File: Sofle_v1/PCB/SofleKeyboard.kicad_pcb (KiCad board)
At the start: 2 copper layers, 137.2 x 109.2 mm, 87 parts, among them J1 LED, J2 4PIN, J3 OLED, P1 i2c_pin, P2 i2c_pin, SW1 SW_PUSH, SW10 SW_PUSH, SW11 SW_PUSH, SW12 SW_PUSH, SW13 SW_PUSH, SW14 SW_PUSH, SW15 SW_PUSH, SW16 SW_PUSH, SW17 SW_PUSH, SW18 SW_PUSH, SW19 SW_PUSH, SW2 SW_PUSH, SW20 SW_PUSH, SW21 SW_PUSH, SW22 SW_PUSH, SW23 SW_PUSH, SW24 SW_PUSH, SW25 Rotary_Encoder_Switch, SW26 SW_PUSH, SW27 SW_PUSH, SW28 SW_PUSH, SW29 SW_PUSH, SW3 SW_PUSH, SW30 SW_PUSH, SW4 SW_PUSH, SW5 SW_PUSH, SW6 SW_PUSH, SW7 SW_PUSH, SW8 SW_PUSH, SW9 SW_PUSH, U1 ProMicro

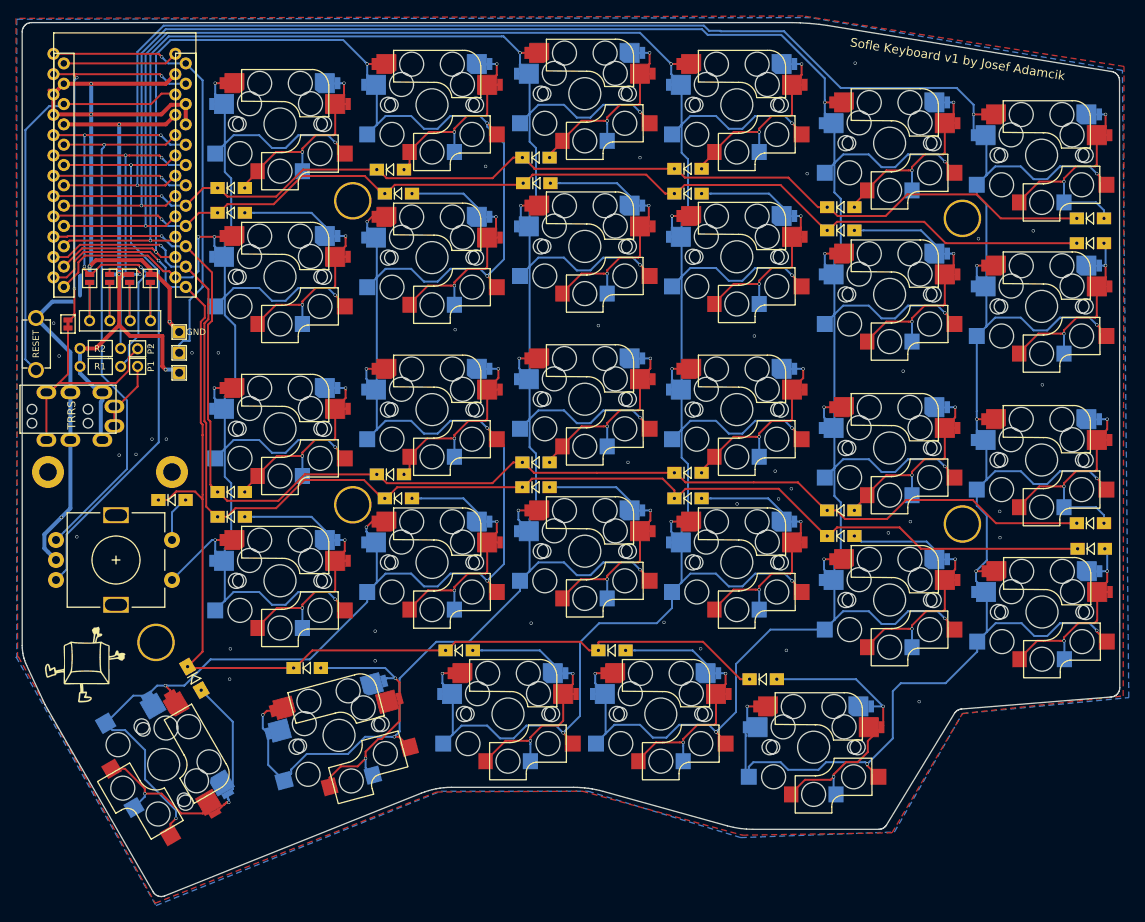
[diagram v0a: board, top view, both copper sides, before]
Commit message: Removed kailh support from the switch footprint
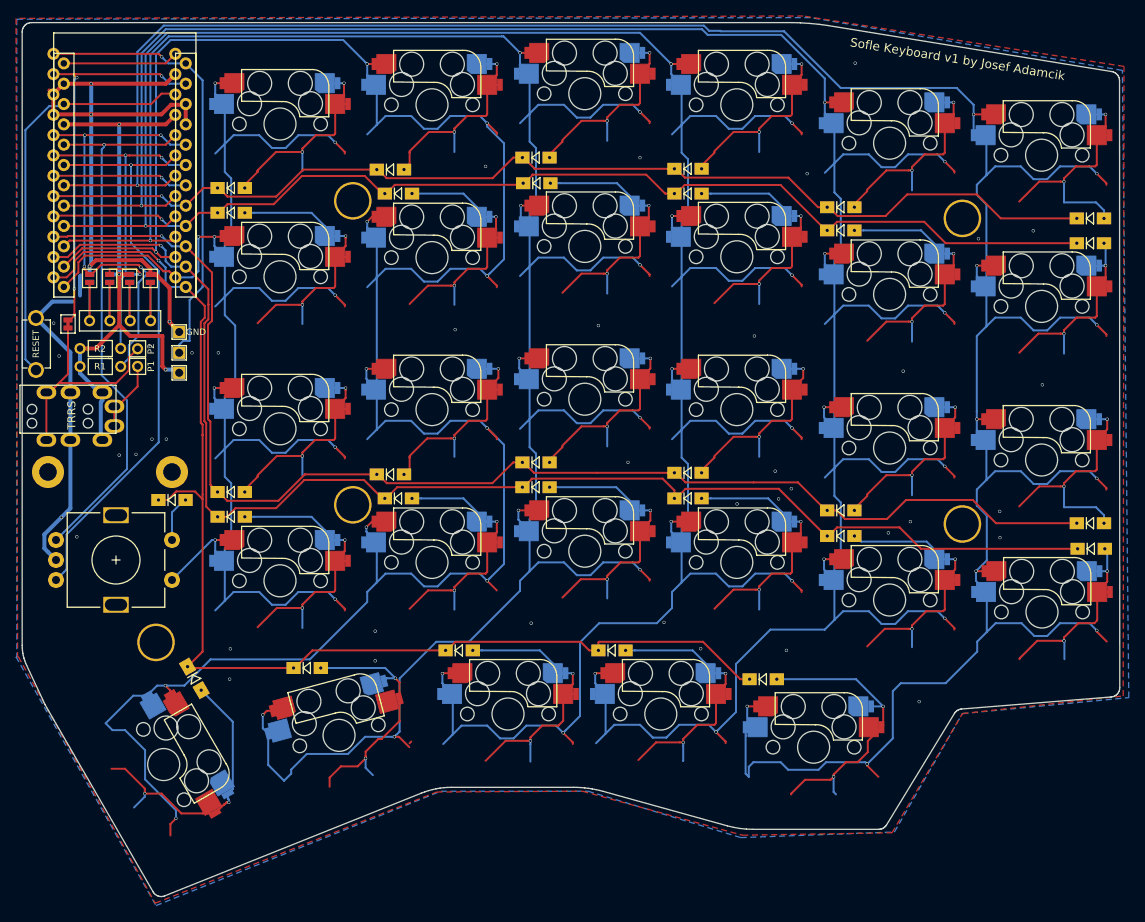
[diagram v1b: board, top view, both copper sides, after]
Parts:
- removed Ref** (x2): Val**, SofleKeyboard-footprint:SofleLogoSmall
- SW1, SW10, SW11, SW12, SW13, SW14, SW15, SW16, SW17, SW18, SW19, SW2, SW20, SW21, SW22, SW23, SW24, SW27, SW28, SW29, SW3, SW30, SW4, SW5, SW6, SW7, SW8, SW9: footprint SofleKeyboard-footprint:CherryMX_KailhLowProfile_Hotswap -> SofleKeyboard-footprint:CherryMX_Hotswap
- SW26: footprint SofleKeyboard-footprint:CherryMX_KailhLowProfile_Hotswap_1.5 -> SofleKeyboard-footprint:CherryMX_Hotswap

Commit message: Fixed routing after footprint change
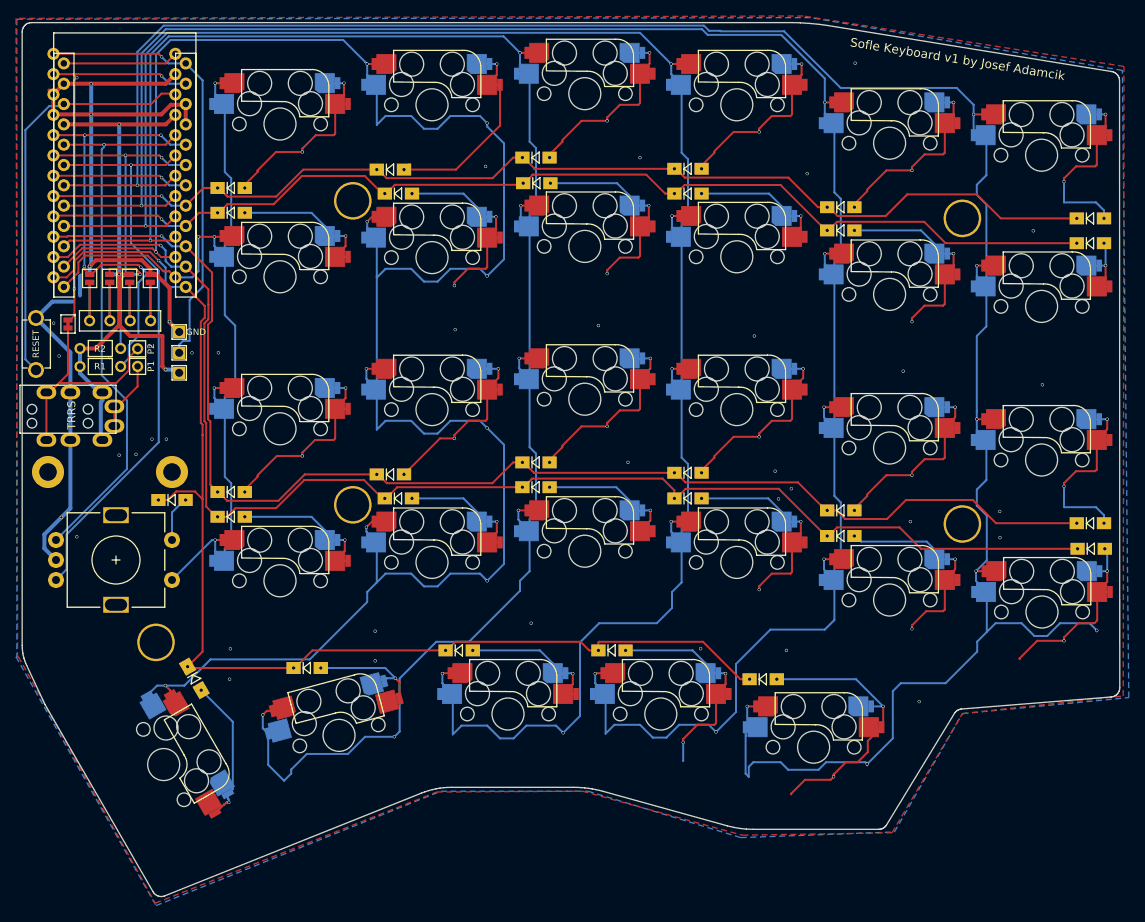
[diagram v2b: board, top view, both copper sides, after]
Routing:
- net SW25A: track 206.1 -> 122.8 mm, vias 9 -> 5
- net col1: track 350.6 -> 270.6 mm, vias 11 -> 7
- net col2: track 334.4 -> 254.3 mm, vias 11 -> 7
- net col3: track 314.7 -> 235.5 mm, vias 11 -> 7
- net col0: track 358.0 -> 300.7 mm, vias 11 -> 8
- net col4: track 311.0 -> 273.0 mm, vias 11 -> 10
- net Net-(D27-Pad2): track 32.8 -> 14.2 mm, vias 2 -> 1
- net Net-(D19-Pad2): track 37.2 -> 19.1 mm, vias 2 -> 1
- net Net-(D12-Pad2): track 28.0 -> 9.92 mm, vias 2 -> 1
- net Net-(D10-Pad2): track 37.0 -> 18.9 mm, vias 2 -> 1
- net Net-(D28-Pad2): track 37.1 -> 19.1 mm, vias 2 -> 1
- net Net-(D21-Pad2): track 37.2 -> 19.2 mm, vias 2 -> 1
- net Net-(D20-Pad2): track 35.2 -> 17.2 mm, vias 2 -> 1
- net Net-(D7-Pad2): track 37.3 -> 19.3 mm, vias 2 -> 1
- net Net-(D26-Pad2): track 36.4 -> 18.5 mm, vias 2 -> 1
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
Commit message: Done with the scheme and positioning of the footprints. Started drawing the tracks
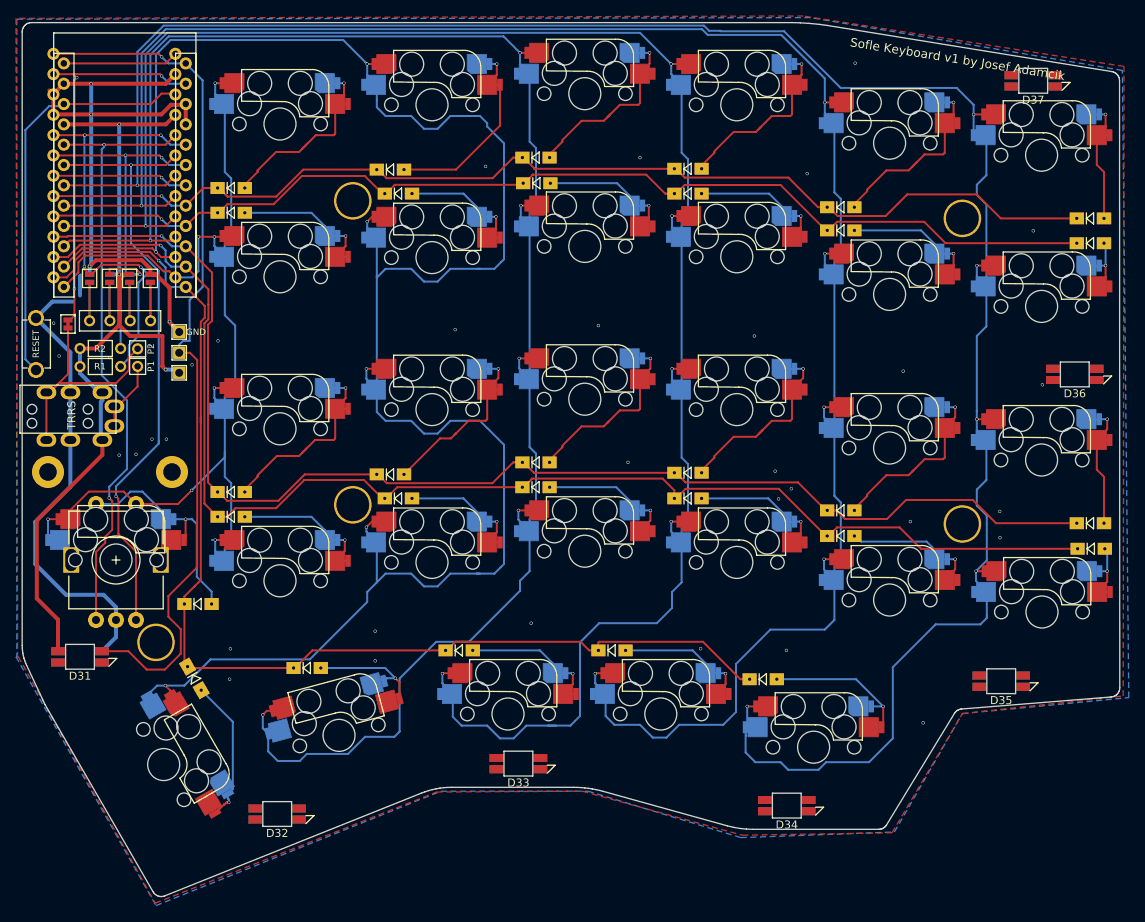
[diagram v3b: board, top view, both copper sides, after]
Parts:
- added D31: SK6812MINI, footprints:YS-SK6812MINI-E_backlight, F.Cu at (95.5, 116.6)
- added D32: SK6812MINI, footprints:YS-SK6812MINI-E_backlight, F.Cu at (120.2, 136.2)
- added D33: SK6812MINI, footprints:YS-SK6812MINI-E_backlight, F.Cu at (150.3, 129.9)
- added D34: SK6812MINI, footprints:YS-SK6812MINI-E_backlight, F.Cu at (183.8, 135.2)
- added D35: SK6812MINI, footprints:YS-SK6812MINI-E_backlight, F.Cu at (210.7, 119.7)
- added D36: SK6812MINI, footprints:YS-SK6812MINI-E_backlight, F.Cu at (219.8, 81.3)
- added D37: SK6812MINI, footprints:YS-SK6812MINI-E_backlight, F.Cu at (214.7, 44.6)
- added SW31: SW_PUSH, SofleKeyboard-footprint:CherryMX_Hotswap, F.Cu at (100.0, 104.5)
- moved D25 13.4 mm to (110.2, 110.0)
- turned SW25 to 90 degrees
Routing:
- net LED: track 55.8 -> 108.9 mm
- net VCC: track 74.2 -> 105.1 mm
- net SW25A: track 122.8 -> 145.6 mm, vias 5 -> 7
- net SW25B: track 5.79 -> 28.4 mm, vias 0 -> 1
- net col0: track 300.7 -> 280.5 mm, vias 8 -> 6
- net GND: track 124.4 -> 143.4 mm, vias 41 -> 39
- net Net-(D30-Pad2): track 34.7 -> 18.9 mm, vias 2 -> 1
- net Net-(D24-Pad2): track 25.9 -> 10.2 mm, vias 2 -> 1
- net Net-(D29-Pad2): track 30.4 -> 19.1 mm, vias 2 -> 1
- net Net-(D23-Pad2): track 28.3 -> 19.2 mm, vias 2 -> 1
- net Net-(D8-Pad2): track 26.1 -> 17.0 mm, vias 2 -> 1
- net Net-(D9-Pad2): track 27.8 -> 18.8 mm, vias 2 -> 1
- net Net-(D22-Pad2): track 28.0 -> 19.0 mm, vias 2 -> 1
- net Net-(D11-Pad2): track 28.0 -> 19.0 mm, vias 2 -> 1
- net ENCA: track 69.0 -> 77.2 mm, vias 1 -> 2
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
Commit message: Done with the routing tracks in Sofle v1
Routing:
- net VCC: track 105.1 -> 368.9 mm, vias 3 -> 13
- net Net-(D35-Pad2): track 0.00 -> 74.5 mm, vias 0 -> 2
- net Net-(D31-Pad2): track 0.00 -> 60.4 mm, vias 0 -> 2
- net Net-(D33-Pad2): track 0.00 -> 58.4 mm, vias 0 -> 2
- net Net-(D32-Pad2): track 0.00 -> 53.4 mm, vias 0 -> 2
- net Net-(D36-Pad2): track 0.00 -> 52.8 mm, vias 0 -> 2
- net Net-(D34-Pad2): track 0.00 -> 52.8 mm, vias 0 -> 2
- net GND: track 143.4 -> 176.3 mm, vias 39 -> 64
- net Net-(D37-Pad2): track 0.00 -> 7.02 mm, vias 0 -> 1
- net col0: track 280.5 -> 287.3 mm, vias 6 -> 8
- net LED: track 108.9 -> 113.5 mm, vias 1 -> 2
